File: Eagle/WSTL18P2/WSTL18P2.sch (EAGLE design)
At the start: 23 parts, among them CON1 1X6CONN-1.27-ROUND, CON2 1X6CONN-1.27-ROUND, CON3 1X6CONN-1.27-ROUND, CON4 1X6CONN-1.27-ROUND, T1 ABS07AIG

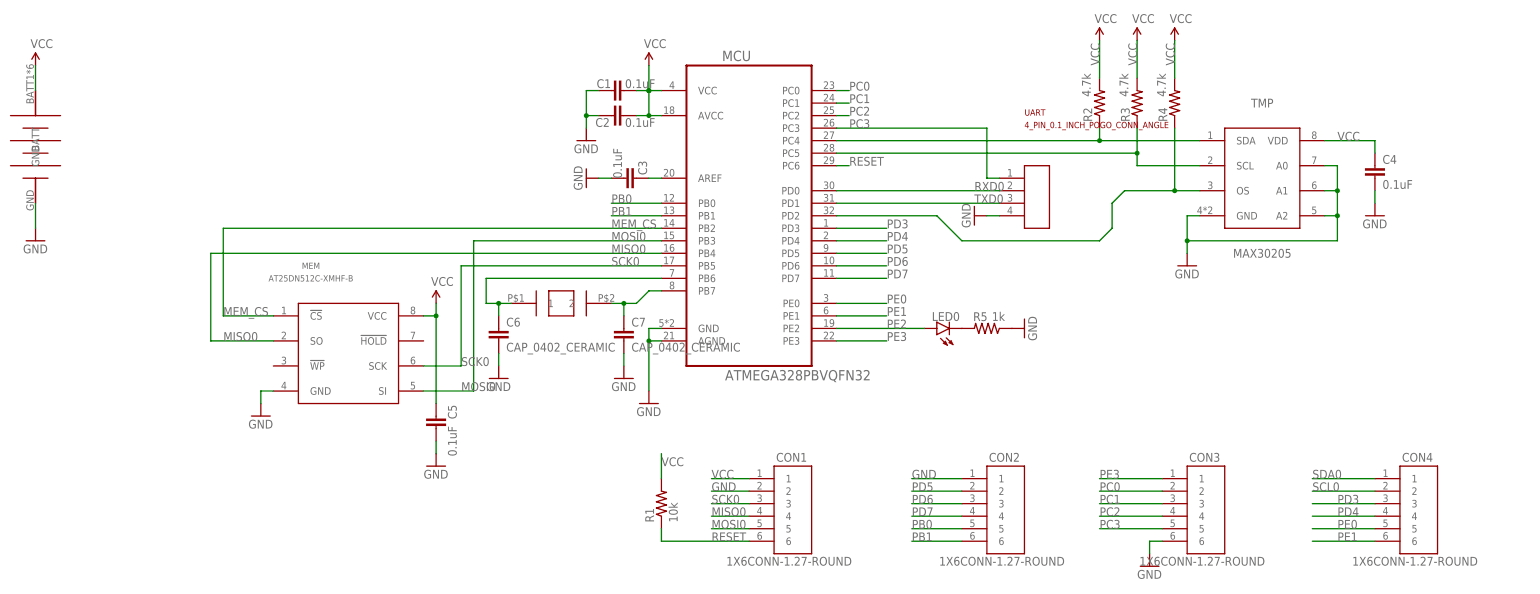
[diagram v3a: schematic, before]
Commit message: Eliminated all 0201 passives, changed uart connection pin
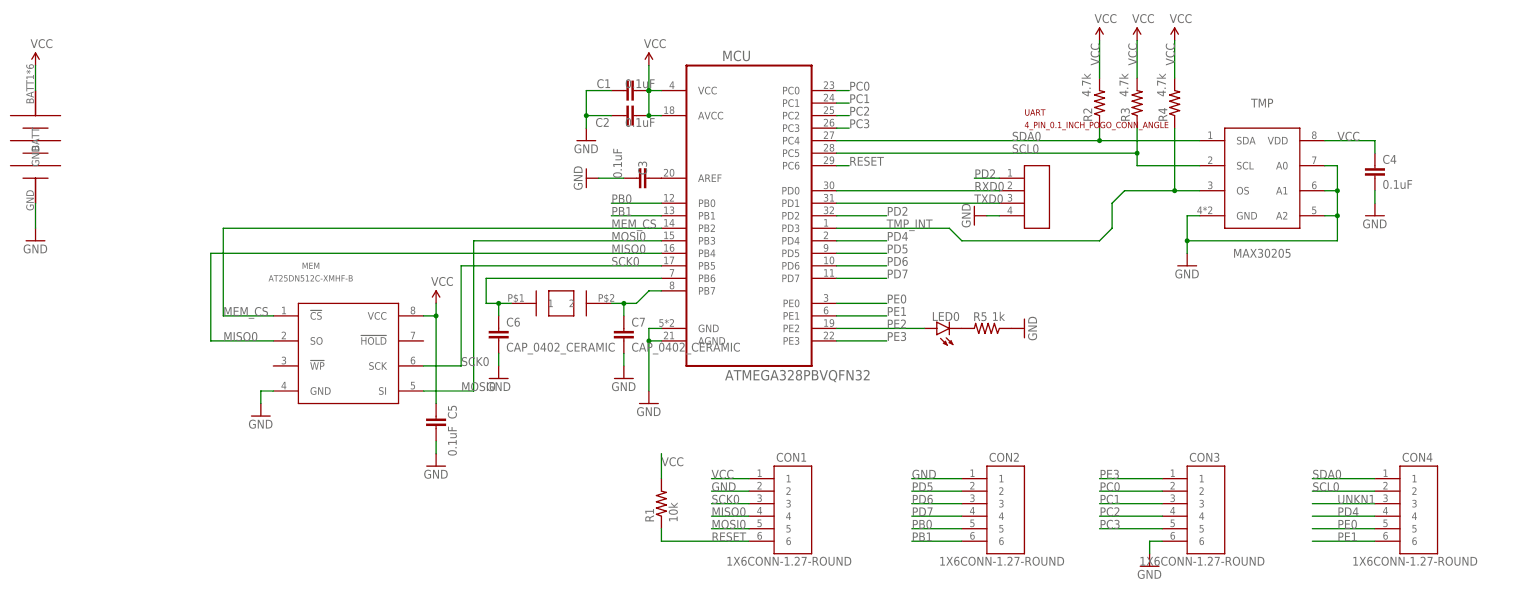
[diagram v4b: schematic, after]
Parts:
- C1, C2, C3: device Passives:CAP_0201_CERAMIC -> Passives:CAP_0402
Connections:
- removed net PD3: CON4.3, MCU.PD3
- new net PD2: MCU.PD2, UART.1
- new net UNKN1: CON4.3
- net PC3: no longer UART.1
- net TMP_INT: now also MCU.PD3; no longer MCU.PD2
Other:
- moved on the sheet: C1, C2, C3
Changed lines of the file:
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@@
 <part name="MCU" library="ATMEGA328PB" deviceset="ATMEGA328PB" device="VQFN32"/>
 <part name="T1" library="ABS07AIG" deviceset="ABS07AIG" device=""/>
-<part name="C1" library="Passives" deviceset="CAP_0201_CERAMIC" device="" value="0.1uF"/>
-<part name="C2" library="Passives" deviceset="CAP_0201_CERAMIC" device="" value="0.1uF"/>
+<part name="C1" library="Passives" deviceset="CAP_0402" device="" value="0.1uF"/>
+<part name="C2" library="Passives" deviceset="CAP_0402" device="" value="0.1uF"/>
 <part name="GND27" library="SparkFun-Aesthetics" deviceset="GND" device=""/>
 <part name="GND1" library="SparkFun-Aesthetics" deviceset="GND" device=""/>
-<part name="C3" library="Passives" deviceset="CAP_0201_CERAMIC" device="" value="0.1uF"/>
+<part name="C3" library="Passives" deviceset="CAP_0402" device="" value="0.1uF"/>
 <part name="GND3" library="SparkFun-Aesthetics" deviceset="GND" device=""/>
 <part name="TMP" library="MAX30205" deviceset="MAX30205" device=""/>
@@
 <wire x1="139.7" y1="60.96" x2="86.36" y2="60.96" width="0.1524" layer="91"/>
 <junction x="139.7" y="60.96"/>
+<label x="121.92" y="60.96" size="1.778" layer="95"/>
 </segment>
 <segment>
@@
 <wire x1="147.32" y1="63.5" x2="147.32" y2="58.42" width="0.1524" layer="91"/>
 <junction x="147.32" y="58.42"/>
+<label x="121.92" y="58.42" size="1.778" layer="95"/>
 </segment>
 <segment>
@@
 <wire x1="48.26" y1="66.04" x2="48.26" y2="71.12" width="0.1524" layer="91"/>
 <pinref part="C1" gate="G$1" pin="1"/>
-<wire x1="45.72" y1="71.12" x2="48.26" y2="71.12" width="0.1524" layer="91"/>
 <junction x="48.26" y="71.12"/>
 <pinref part="C2" gate="G$1" pin="1"/>
-<wire x1="45.72" y1="66.04" x2="48.26" y2="66.04" width="0.1524" layer="91"/>
 <junction x="48.26" y="66.04"/>
 <wire x1="48.26" y1="76.2" x2="48.26" y2="71.12" width="0.1524" layer="91"/>
@@
 <pinref part="C1" gate="G$1" pin="2"/>
 <pinref part="GND27" gate="1" pin="GND"/>
-<wire x1="38.1" y1="71.12" x2="35.56" y2="71.12" width="0.1524" layer="91"/>
+<wire x1="40.64" y1="71.12" x2="35.56" y2="71.12" width="0.1524" layer="91"/>
 <wire x1="35.56" y1="71.12" x2="35.56" y2="66.04" width="0.1524" layer="91"/>
 <pinref part="C2" gate="G$1" pin="2"/>
 <wire x1="35.56" y1="66.04" x2="35.56" y2="63.5" width="0.1524" layer="91"/>
-<wire x1="38.1" y1="66.04" x2="35.56" y2="66.04" width="0.1524" layer="91"/>
+<wire x1="40.64" y1="66.04" x2="35.56" y2="66.04" width="0.1524" layer="91"/>
 <junction x="35.56" y="66.04"/>
 </segment>
@@
 <pinref part="GND3" gate="1" pin="GND"/>
 <pinref part="C3" gate="G$1" pin="2"/>
-<wire x1="38.1" y1="53.34" x2="40.64" y2="53.34" width="0.1524" layer="91"/>
+<wire x1="38.1" y1="53.34" x2="43.18" y2="53.34" width="0.1524" layer="91"/>
 </segment>
 <segment>
@@
 <pinref part="C3" gate="G$1" pin="1"/>
 <pinref part="MCU" gate="A" pin="AREF"/>
-<wire x1="48.26" y1="53.34" x2="50.8" y2="53.34" width="0.1524" layer="91"/>
 </segment>
 </net>
@@
 <segment>
 <pinref part="R4" gate="G$1" pin="2"/>
-<pinref part="MCU" gate="A" pin="PD2"/>
-<wire x1="86.36" y1="45.72" x2="106.68" y2="45.72" width="0.1524" layer="91"/>
-<wire x1="106.68" y1="45.72" x2="111.76" y2="40.64" width="0.1524" layer="91"/>
+<wire x1="109.22" y1="43.18" x2="111.76" y2="40.64" width="0.1524" layer="91"/>
 <wire x1="111.76" y1="40.64" x2="139.7" y2="40.64" width="0.1524" layer="91"/>
 <wire x1="139.7" y1="40.64" x2="142.24" y2="43.18" width="0.1524" layer="91"/>
@@
 <wire x1="154.94" y1="63.5" x2="154.94" y2="50.8" width="0.1524" layer="91"/>
 <junction x="154.94" y="50.8"/>
+<pinref part="MCU" gate="A" pin="PD3"/>
+<wire x1="86.36" y1="43.18" x2="109.22" y2="43.18" width="0.1524" layer="91"/>
+<label x="96.52" y="43.18" size="1.778" layer="95"/>
 </segment>
 </net>
@@
 <pinref part="LED0" gate="G$1" pin="C"/>
 <pinref part="R5" gate="G$1" pin="1"/>
-</segment>
-</net>
-<net name="PD3" class="0">
-<segment>
-<pinref part="MCU" gate="A" pin="PD3"/>
-<wire x1="86.36" y1="43.18" x2="96.52" y2="43.18" width="0.1524" layer="91"/>
-<label x="96.52" y="43.18" size="1.778" layer="95"/>
-</segment>
-<segment>
-<label x="187.96" y="-12.7" size="1.778" layer="95"/>
-<wire x1="182.88" y1="-12.7" x2="195.58" y2="-12.7" width="0.1524" layer="91"/>
-<pinref part="CON4" gate="G$1" pin="3"/>
 </segment>
 </net>
@@
 <pinref part="MCU" gate="A" pin="PC3"/>
 <label x="88.9" y="63.5" size="1.778" layer="95"/>
-<wire x1="86.36" y1="63.5" x2="116.84" y2="63.5" width="0.1524" layer="91"/>
-<wire x1="116.84" y1="63.5" x2="116.84" y2="53.34" width="0.1524" layer="91"/>
-<pinref part="UART" gate="G$1" pin="1"/>
-<wire x1="116.84" y1="53.34" x2="119.38" y2="53.34" width="0.1524" layer="91"/>
+<wire x1="86.36" y1="63.5" x2="88.9" y2="63.5" width="0.1524" layer="91"/>
 </segment>
 <segment>
@@
 </segment>
 </net>
+<net name="UNKN1" class="0">
+<segment>
+<label x="187.96" y="-12.7" size="1.778" layer="95"/>
+<wire x1="182.88" y1="-12.7" x2="195.58" y2="-12.7" width="0.1524" layer="91"/>
+<pinref part="CON4" gate="G$1" pin="3"/>
+</segment>
+</net>
+<net name="PD2" class="0">
+<segment>
+<pinref part="MCU" gate="A" pin="PD2"/>
+<wire x1="86.36" y1="45.72" x2="96.52" y2="45.72" width="0.1524" layer="91"/>
+<label x="96.52" y="45.72" size="1.778" layer="95"/>
+</segment>
+<segment>
+<pinref part="UART" gate="G$1" pin="1"/>
+<wire x1="119.38" y1="53.34" x2="114.3" y2="53.34" width="0.1524" layer="91"/>
+<label x="114.3" y="53.34" size="1.778" layer="95"/>
+</segment>
+</net>
